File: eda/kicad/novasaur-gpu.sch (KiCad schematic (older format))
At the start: 24 parts, among them U1 74F86, U28 74F163, U29 74F163, U3 74F11, U30 74F541, U31 74F574, U32 74F574, U33 74F541, U34 74F574, U35 74F299, U36 74F574, U37 74F157

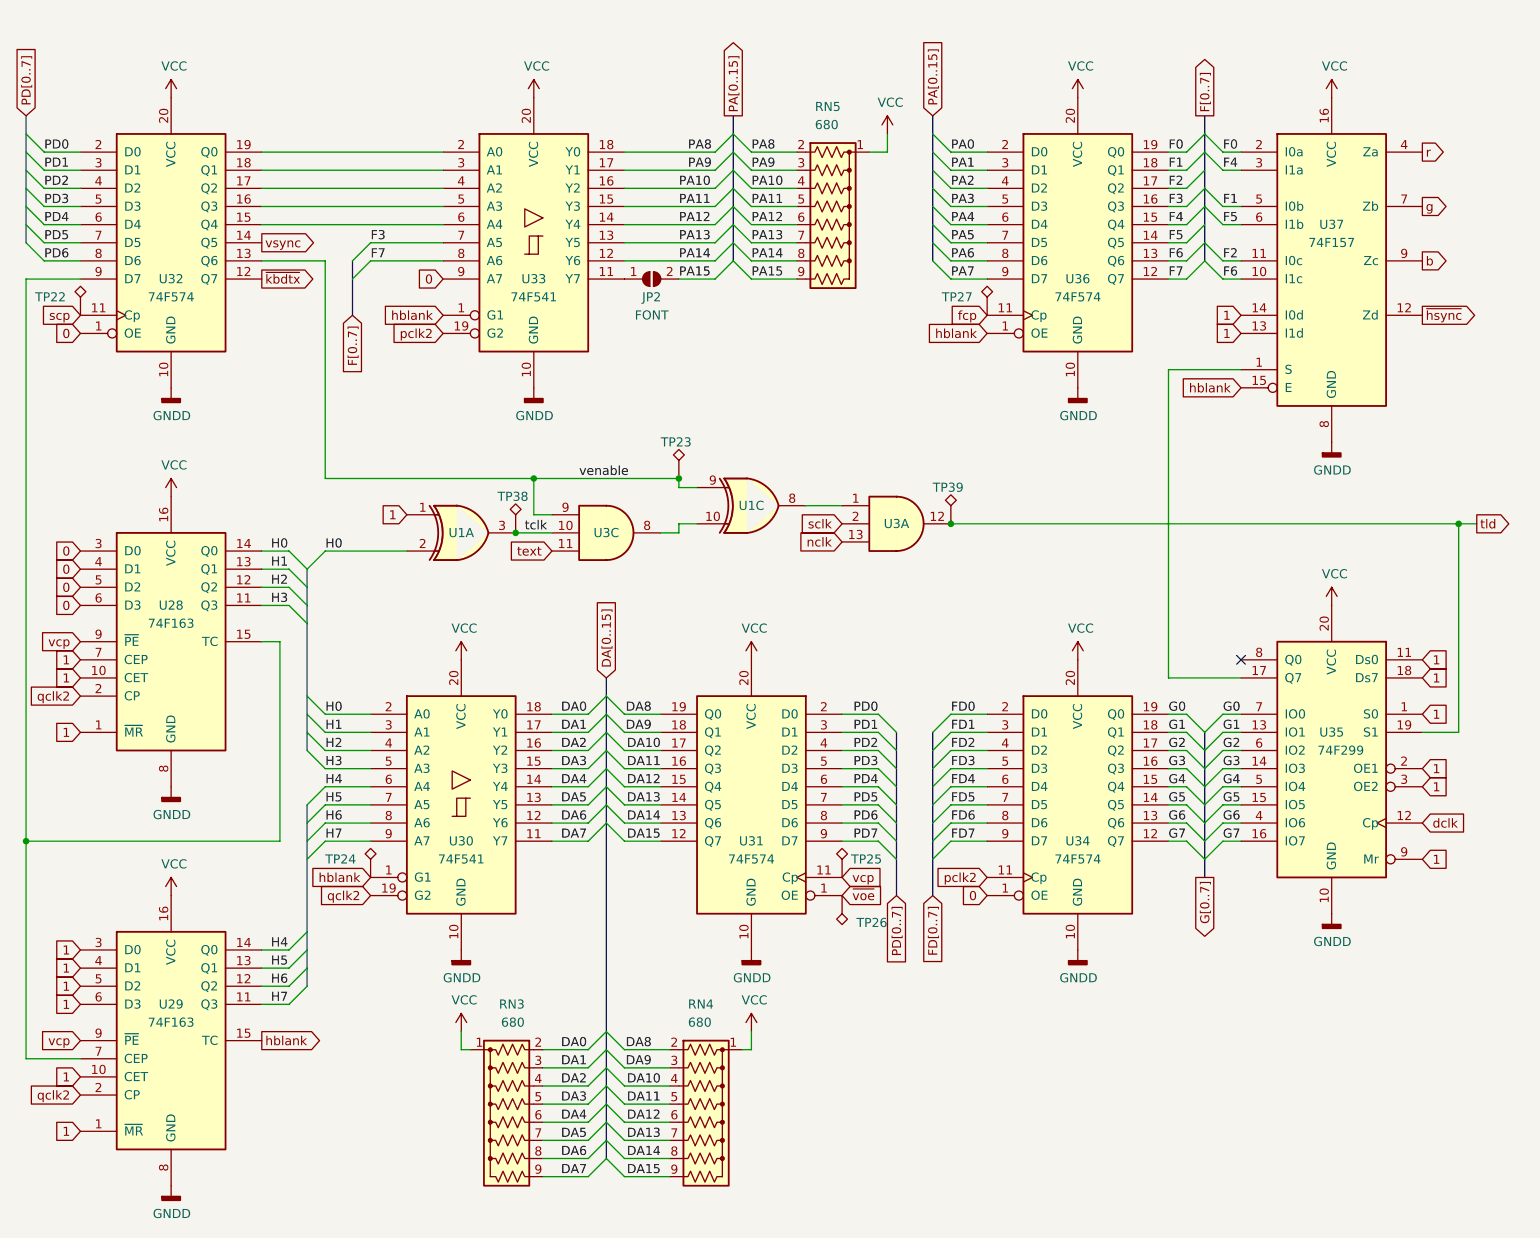
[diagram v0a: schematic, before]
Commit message: add TVS diode ESD protection
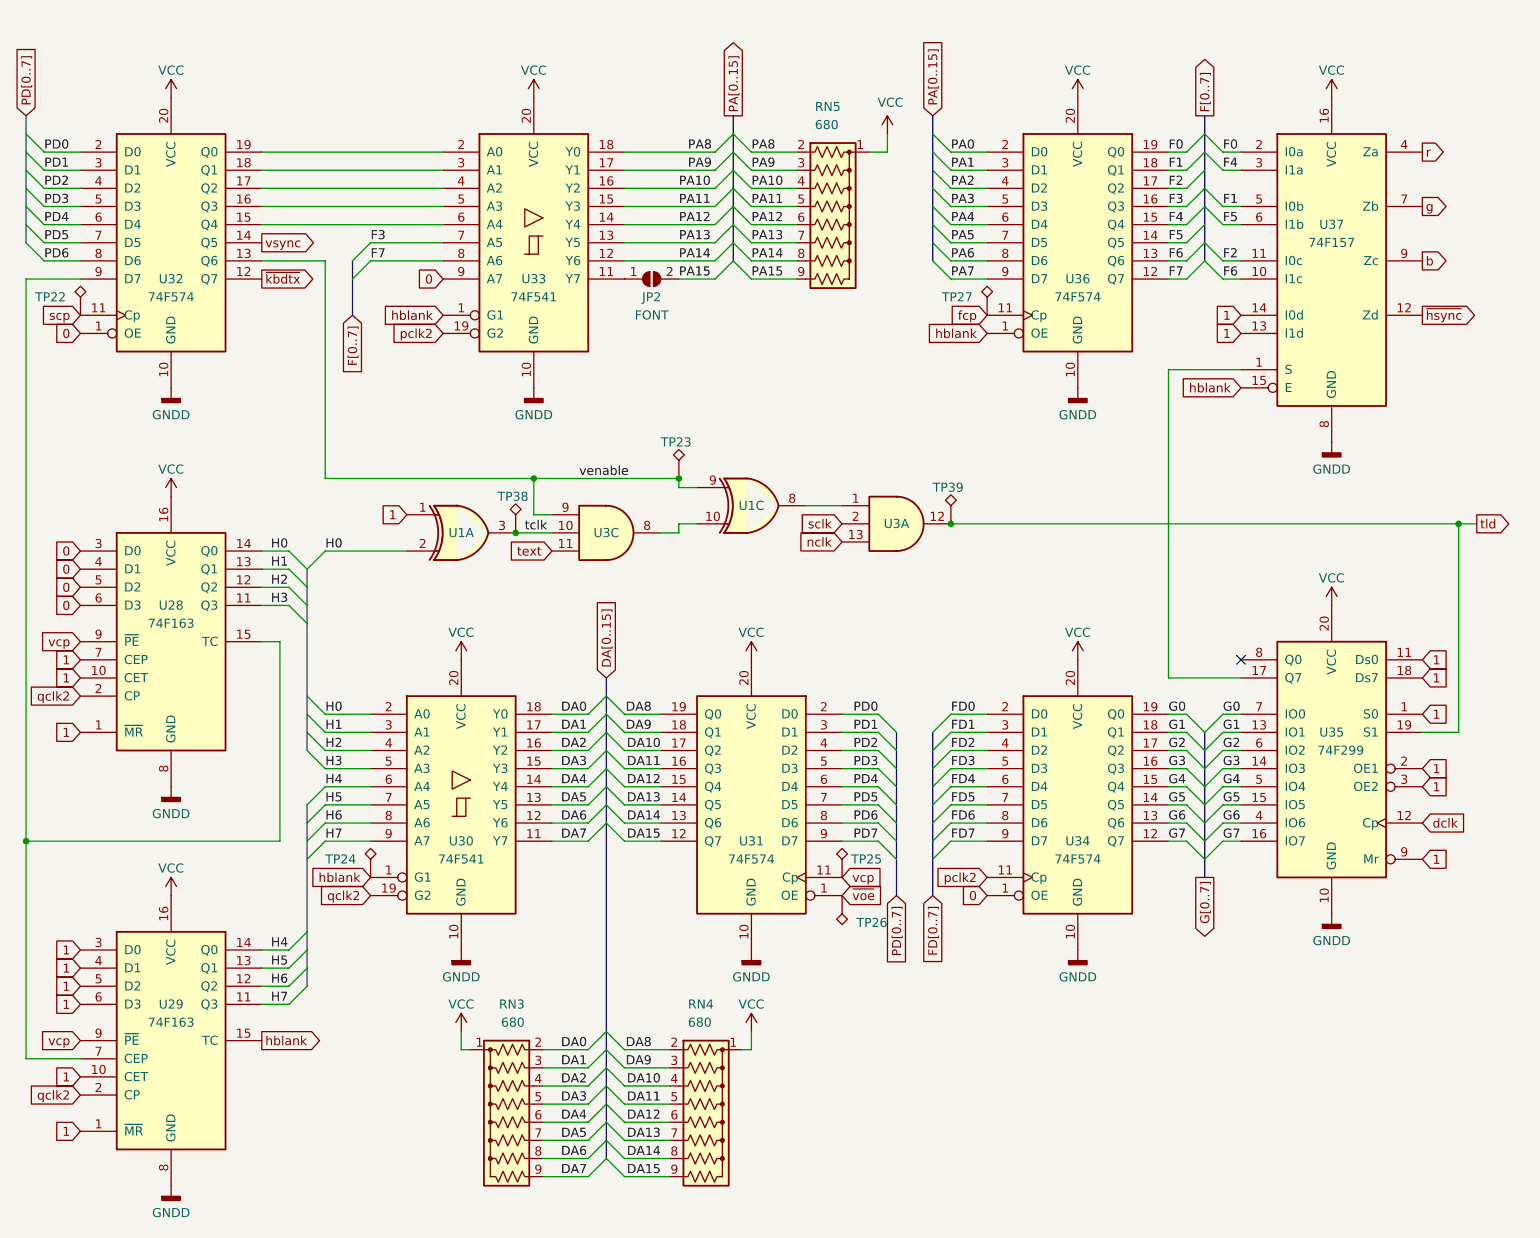
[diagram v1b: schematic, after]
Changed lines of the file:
@@
 Sheet 3 4
 Title "Graphics Processing Unit"
-Date "2021-06-06"
-Rev "1.9"
+Date "2021-07-10"
+Rev "1.10"
 Comp ""
 Comment1 "(c) Solid State Machines 2021"
@@
 AR Path="/5DA1E9BD/5D7DF376" Ref="#PWR0155"  Part="1"
 F 0 "#PWR0155" H 2200 2600 50  0001 C CNN
-F 1 "GNDD" H 2204 2695 50  0000 C CNN
+F 1 "GNDD" H 2200 2700 50  0000 C CNN
 F 2 "" H 2200 2850 50  0001 C CNN
 F 3 "" H 2200 2850 50  0001 C CNN
@@
 AR Path="/5DA1E9BD/5D7D093F" Ref="#PWR0156"  Part="1"
 F 0 "#PWR0156" H 2200 1100 50  0001 C CNN
-F 1 "VCC" H 2217 1423 50  0000 C CNN
+F 1 "VCC" H 2200 1400 50  0000 C CNN
 F 2 "" H 2200 1250 50  0001 C CNN
 F 3 "" H 2200 1250 50  0001 C CNN
@@
 AR Path="/5DA1E9BD/621DFBC5" Ref="#PWR0158"  Part="1"
 F 0 "#PWR0158" H 4200 1100 50  0001 C CNN
-F 1 "VCC" H 4217 1423 50  0000 C CNN
+F 1 "VCC" H 4200 1400 50  0000 C CNN
 F 2 "" H 4200 1250 50  0001 C CNN
 F 3 "" H 4200 1250 50  0001 C CNN
@@
 AR Path="/5DA1E9BD/5F0FA20D" Ref="#PWR0157"  Part="1"
 F 0 "#PWR0157" H 4200 2600 50  0001 C CNN
-F 1 "GNDD" H 4204 2695 50  0000 C CNN
+F 1 "GNDD" H 4200 2700 50  0000 C CNN
 F 2 "" H 4200 2850 50  0001 C CNN
 F 3 "" H 4200 2850 50  0001 C CNN
@@
 AR Path="/5DA1E9BD/621DEBCC" Ref="#PWR0152"  Part="1"
 F 0 "#PWR0152" H 8600 1100 50  0001 C CNN
-F 1 "VCC" H 8617 1423 50  0000 C CNN
+F 1 "VCC" H 8600 1400 50  0000 C CNN
 F 2 "" H 8600 1250 50  0001 C CNN
 F 3 "" H 8600 1250 50  0001 C CNN
@@
 AR Path="/5DA1E9BD/621DDA78" Ref="#PWR0151"  Part="1"
 F 0 "#PWR0151" H 7200 1100 50  0001 C CNN
-F 1 "VCC" H 7217 1423 50  0000 C CNN
+F 1 "VCC" H 7200 1400 50  0000 C CNN
 F 2 "" H 7200 1250 50  0001 C CNN
 F 3 "" H 7200 1250 50  0001 C CNN
@@
 AR Path="/5DA1E9BD/60936E83" Ref="#PWR0150"  Part="1"
 F 0 "#PWR0150" H 7200 2600 50  0001 C CNN
-F 1 "GNDD" H 7204 2695 50  0000 C CNN
+F 1 "GNDD" H 7200 2700 50  0000 C CNN
 F 2 "" H 7200 2850 50  0001 C CNN
 F 3 "" H 7200 2850 50  0001 C CNN
@@
 AR Path="/5DA1E9BD/5F15FC9A" Ref="#PWR0163"  Part="1"
 F 0 "#PWR0163" H 7200 5700 50  0001 C CNN
-F 1 "GNDD" H 7204 5795 50  0000 C CNN
+F 1 "GNDD" H 7200 5800 50  0000 C CNN
 F 2 "" H 7200 5950 50  0001 C CNN
 F 3 "" H 7200 5950 50  0001 C CNN
@@
 AR Path="/5DA1E9BD/5E4DC06C" Ref="#PWR0143"  Part="1"
 F 0 "#PWR0143" H 2200 5500 50  0001 C CNN
-F 1 "VCC" H 2217 5823 50  0000 C CNN
+F 1 "VCC" H 2200 5800 50  0000 C CNN
 F 2 "" H 2200 5650 50  0001 C CNN
 F 3 "" H 2200 5650 50  0001 C CNN
@@
 AR Path="/5DA1E9BD/5E4E6308" Ref="#PWR0144"  Part="1"
 F 0 "#PWR0144" H 3800 4200 50  0001 C CNN
-F 1 "VCC" H 3817 4523 50  0000 C CNN
+F 1 "VCC" H 3800 4500 50  0000 C CNN
 F 2 "" H 3800 4350 50  0001 C CNN
 F 3 "" H 3800 4350 50  0001 C CNN
@@
 AR Path="/5DA1E9BD/5E721518" Ref="#PWR0146"  Part="1"
 F 0 "#PWR0146" H 2200 7000 50  0001 C CNN
-F 1 "GNDD" H 2204 7095 50  0000 C CNN
+F 1 "GNDD" H 2200 7100 50  0000 C CNN
 F 2 "" H 2200 7250 50  0001 C CNN
 F 3 "" H 2200 7250 50  0001 C CNN
@@
 AR Path="/5DA1E9BD/5E722349" Ref="#PWR0147"  Part="1"
 F 0 "#PWR0147" H 3800 5700 50  0001 C CNN
-F 1 "GNDD" H 3804 5795 50  0000 C CNN
+F 1 "GNDD" H 3800 5800 50  0000 C CNN
 F 2 "" H 3800 5950 50  0001 C CNN
 F 3 "" H 3800 5950 50  0001 C CNN
@@
 AR Path="/5DA1E9BD/5D1C11D4" Ref="#PWR0153"  Part="1"
 F 0 "#PWR0153" H 5400 6250 50  0001 C CNN
-F 1 "VCC" H 5417 6573 50  0000 C CNN
+F 1 "VCC" H 5400 6550 50  0000 C CNN
 F 2 "" H 5400 6400 50  0001 C CNN
 F 3 "" H 5400 6400 50  0001 C CNN
@@
 AR Path="/5DA1E9BD/5F174359" Ref="#PWR0160"  Part="1"
 F 0 "#PWR0160" H 8600 3900 50  0001 C CNN
-F 1 "VCC" H 8617 4223 50  0000 C CNN
+F 1 "VCC" H 8600 4200 50  0000 C CNN
 F 2 "" H 8600 4050 50  0001 C CNN
 F 3 "" H 8600 4050 50  0001 C CNN
@@
 AR Path="/5DA1E9BD/5F161314" Ref="#PWR0161"  Part="1"
 F 0 "#PWR0161" H 7200 4200 50  0001 C CNN
-F 1 "VCC" H 7217 4523 50  0000 C CNN
+F 1 "VCC" H 7200 4500 50  0000 C CNN
 F 2 "" H 7200 4350 50  0001 C CNN
 F 3 "" H 7200 4350 50  0001 C CNN
@@
 AR Path="/5DA1E9BD/5F160896" Ref="#PWR0162"  Part="1"
 F 0 "#PWR0162" H 8600 5500 50  0001 C CNN
-F 1 "GNDD" H 8604 5595 50  0000 C CNN
+F 1 "GNDD" H 8600 5600 50  0000 C CNN
 F 2 "" H 8600 5750 50  0001 C CNN
 F 3 "" H 8600 5750 50  0001 C CNN
@@
 AR Path="/5DA1E9BD/5E4ED6D8" Ref="#PWR0164"  Part="1"
 F 0 "#PWR0164" H 2200 3300 50  0001 C CNN
-F 1 "VCC" H 2217 3623 50  0000 C CNN
+F 1 "VCC" H 2200 3600 50  0000 C CNN
 F 2 "" H 2200 3450 50  0001 C CNN
 F 3 "" H 2200 3450 50  0001 C CNN
@@
 AR Path="/5DA1E9BD/5E4DB628" Ref="#PWR0165"  Part="1"
 F 0 "#PWR0165" H 2200 4800 50  0001 C CNN
-F 1 "GNDD" H 2204 4895 50  0000 C CNN
+F 1 "GNDD" H 2200 4900 50  0000 C CNN
 F 2 "" H 2200 5050 50  0001 C CNN
 F 3 "" H 2200 5050 50  0001 C CNN
@@
 AR Path="/5DA1E9BD/5E732E82" Ref="#PWR0166"  Part="1"
 F 0 "#PWR0166" H 3800 6250 50  0001 C CNN
-F 1 "VCC" H 3817 6573 50  0000 C CNN
+F 1 "VCC" H 3800 6550 50  0000 C CNN
 F 2 "" H 3800 6400 50  0001 C CNN
 F 3 "" H 3800 6400 50  0001 C CNN
@@
 AR Path="/5DA1E9BD/5DC7B04C" Ref="#PWR0145"  Part="1"
 F 0 "#PWR0145" H 5400 5700 50  0001 C CNN
-F 1 "GNDD" H 5404 5795 50  0000 C CNN
+F 1 "GNDD" H 5400 5800 50  0000 C CNN
 F 2 "" H 5400 5950 50  0001 C CNN
 F 3 "" H 5400 5950 50  0001 C CNN
@@
 AR Path="/5DA1E9BD/5DC90855" Ref="#PWR0148"  Part="1"
 F 0 "#PWR0148" H 5400 4200 50  0001 C CNN
-F 1 "VCC" H 5417 4523 50  0000 C CNN
+F 1 "VCC" H 5400 4500 50  0000 C CNN
 F 2 "" H 5400 4350 50  0001 C CNN
 F 3 "" H 5400 4350 50  0001 C CNN
@@
 AR Path="/5DA1E9BD/5F1A79BE" Ref="#PWR0149"  Part="1"
 F 0 "#PWR0149" H 8600 2900 50  0001 C CNN
-F 1 "GNDD" H 8604 2995 50  0000 C CNN
+F 1 "GNDD" H 8600 3000 50  0000 C CNN
 F 2 "" H 8600 3150 50  0001 C CNN
 F 3 "" H 8600 3150 50  0001 C CNN

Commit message: remove 6v regulator go back to rev.1 do not collect 00
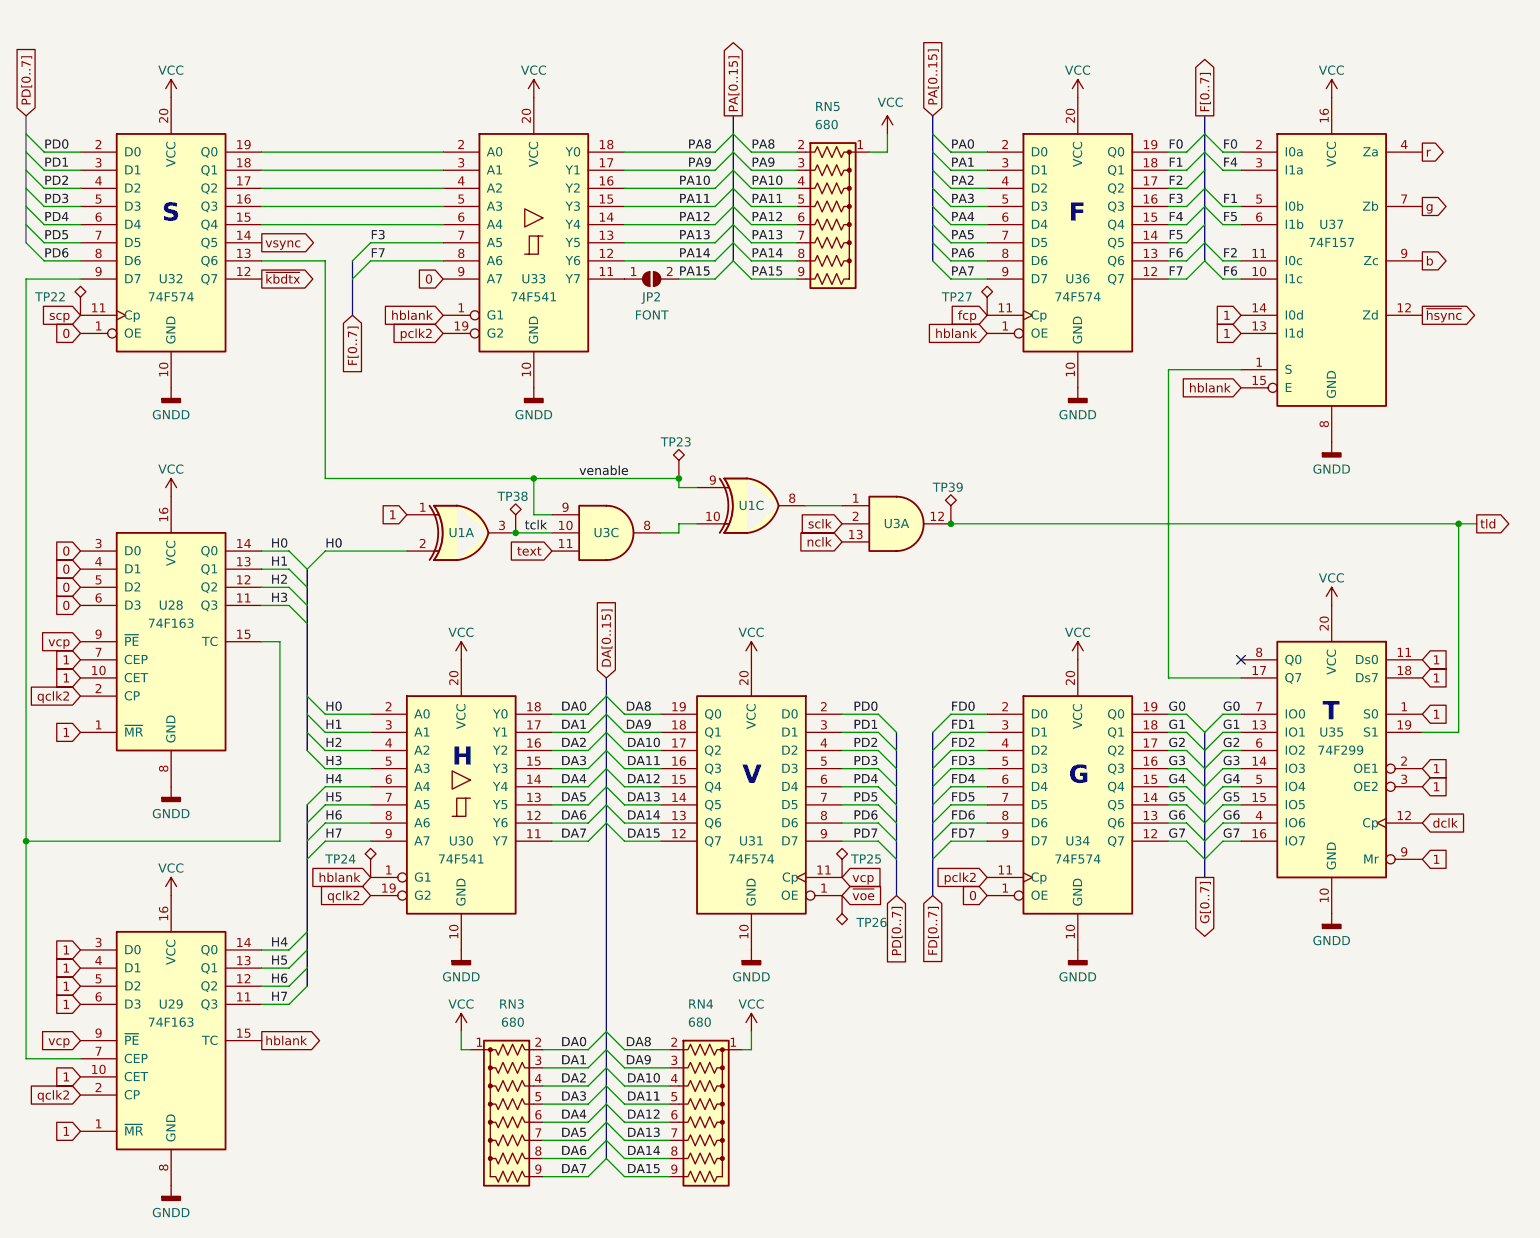
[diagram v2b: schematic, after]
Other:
- note added: "F"
- note added: "G"
- note added: "H"
- note added: "S"
- note added: "T"
- note added: "V"
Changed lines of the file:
@@
 Sheet 3 4
 Title "Graphics Processing Unit"
-Date "2021-07-10"
+Date "2021-08-01"
 Rev "1.10"
 Comp ""
@@
 Wire Wire Line
 	4200 3350 5000 3350
+Text Notes 3750 4950 0    100  ~ 20
+H
+Text Notes 5350 5050 0    100  ~ 20
+V
+Text Notes 7150 1950 0    100  ~ 20
+F
+Text Notes 7150 5050 0    100  ~ 20
+G
+Text Notes 2150 1950 0    100  ~ 20
+S
+Text Notes 8550 4700 0    100  ~ 20
+T
 Wire Bus Line
 	3200 2150 3200 2450

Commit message: Rev. 10 with 5v PSU
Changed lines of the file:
@@
 Sheet 3 4
 Title "Graphics Processing Unit"
-Date "2021-08-01"
+Date "2021-09-02"
 Rev "1.10"
 Comp ""
@@
 Wire Wire Line
 	4200 3350 5000 3350
-Text Notes 3750 4950 0    100  ~ 20
+Text Notes 3750 4950 0    100  ~ 0
 H
-Text Notes 5350 5050 0    100  ~ 20
+Text Notes 5350 5050 0    100  ~ 0
 V
-Text Notes 7150 1950 0    100  ~ 20
+Text Notes 7150 1950 0    100  ~ 0
 F
-Text Notes 7150 5050 0    100  ~ 20
+Text Notes 7150 5050 0    100  ~ 0
 G
-Text Notes 2150 1950 0    100  ~ 20
+Text Notes 2150 1950 0    100  ~ 0
 S
-Text Notes 8550 4700 0    100  ~ 20
+Text Notes 8550 4700 0    100  ~ 0
 T
 Wire Bus Line
